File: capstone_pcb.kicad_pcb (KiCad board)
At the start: 4 copper layers, 60.2 x 43.6 mm, 44 parts, among them IC6 BSS138, Q1 BSS138, U2 BMI270, U3 NRF52840-QIAA-R, U4 MAX30102EFD+T, U5 AMS1117-1.8, U6 TPS61099DRV, X1 32MHz, X2 32.768kHz

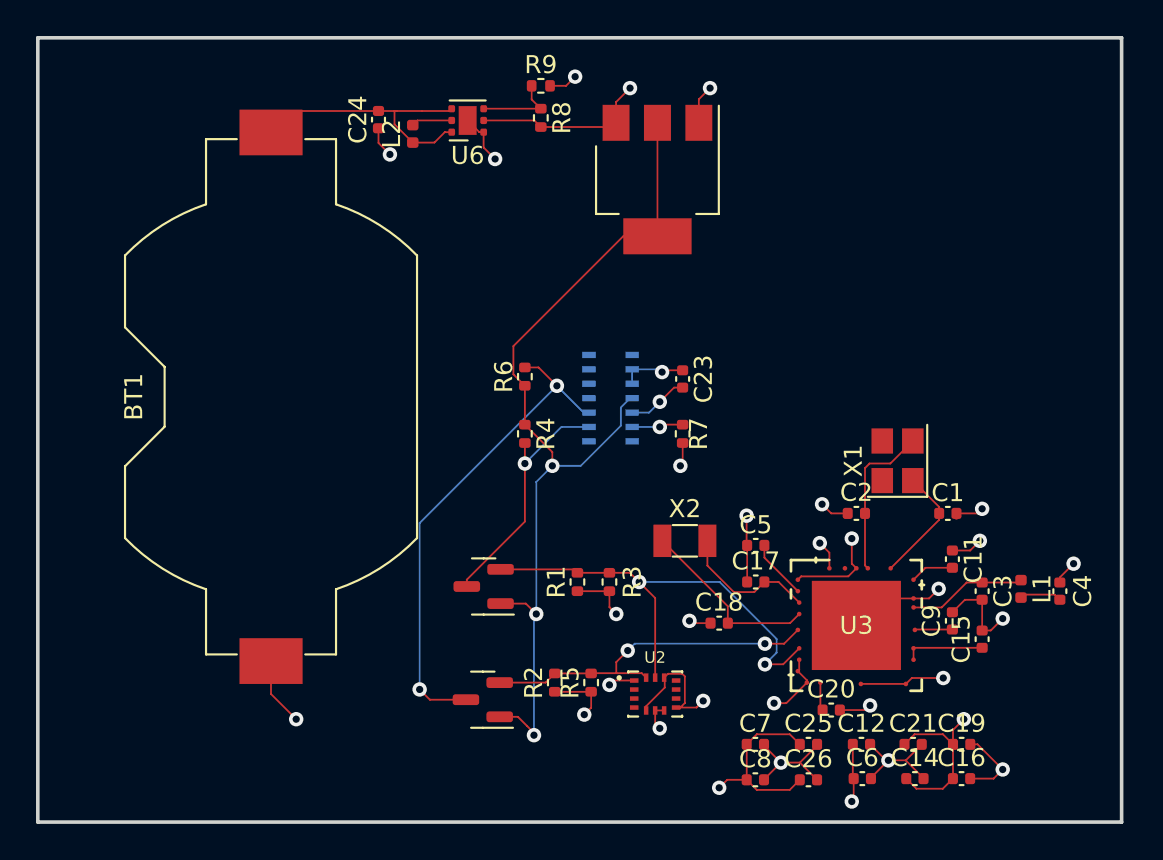
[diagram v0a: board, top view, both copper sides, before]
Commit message: exposed SWD pins and added LED for flashing status
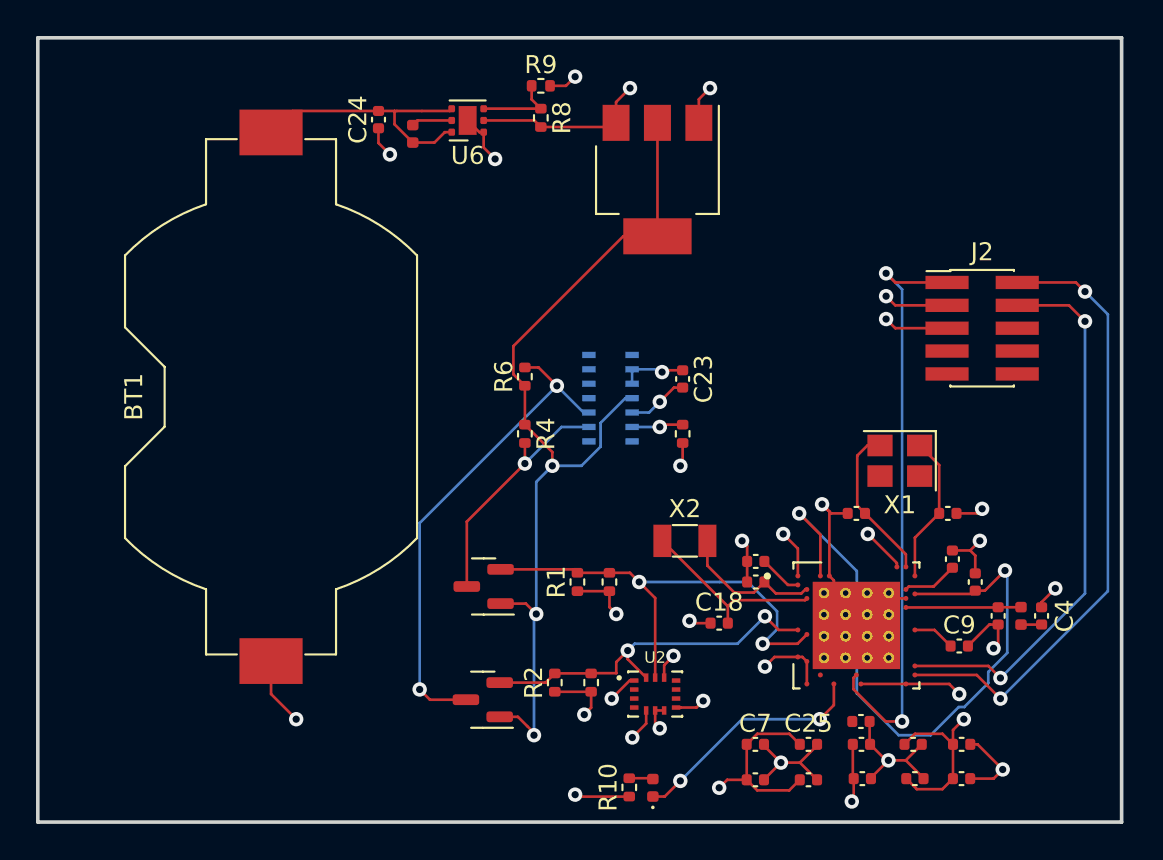
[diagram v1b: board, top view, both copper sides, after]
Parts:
- added D1: LED, LED_SMD:LED_0402_1005Metric, F.Cu at (114.6, 87.4)
- added J2: Conn_01x05_Pin, Connector_PinHeader_1.27mm:PinHeader_2x05_P1.27mm_Vertical_SMD, F.Cu at (132.8, 61.8)
- added R10: 0.4k, Resistor_SMD:R_0402_1005Metric, F.Cu at (113.2, 87.4)
- R3, R4, R5, R6, R7: value 10K -> 10k
- U3: footprint nrf:nrf52840_qiaa_r -> nrf:XCVR_NRF52840-QIAA-R-edited
- moved C15 3.20 mm to (132.5, 75.9)
- moved C20 1.77 mm to (126.1, 83.7)
- moved C4 1.71 mm to (136.1, 77.8)
- moved C3 1.64 mm to (133.7, 77.8)
- moved L1 1.50 mm to (135.0, 77.8)
- moved C9 1.45 mm to (131.6, 79.5), turned to 0 degrees
- moved C5 0.89 mm to (120.3, 74.8)
- moved X1 0.13 mm to (128.3, 69.2), turned to 180 degrees
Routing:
- net Net-(J2-Pin_2): track 0.00 -> 34.9 mm, vias 0 -> 2
- net Net-(J2-Pin_1): track 0.00 -> 33.2 mm, vias 0 -> 2
- net /DEC4 6: track 4.46 -> 37.0 mm, vias 0 -> 2
- net Net-(J2-Pin_4): track 0.00 -> 30.9 mm, vias 0 -> 2
- net Net-(D1-K): track 0.00 -> 13.3 mm, vias 0 -> 2
- net GND: track 61.4 -> 72.9 mm, vias 21 -> 19
- net +3V3: track 62.5 -> 68.0 mm, vias 11 -> 16
- net Net-(U3-XC1): track 6.59 -> 8.25 mm
- net Net-(U3-DECUSB): track 1.57 -> 0.00 mm
- net Net-(D1-A): track 0.00 -> 1.33 mm
- net /RF: track 2.28 -> 1.15 mm
- net Net-(U3-DEC1): track 3.31 -> 2.40 mm
- net /SDA: track 19.9 -> 20.7 mm
- net Net-(U3-DEC3): track 2.43 -> 3.08 mm

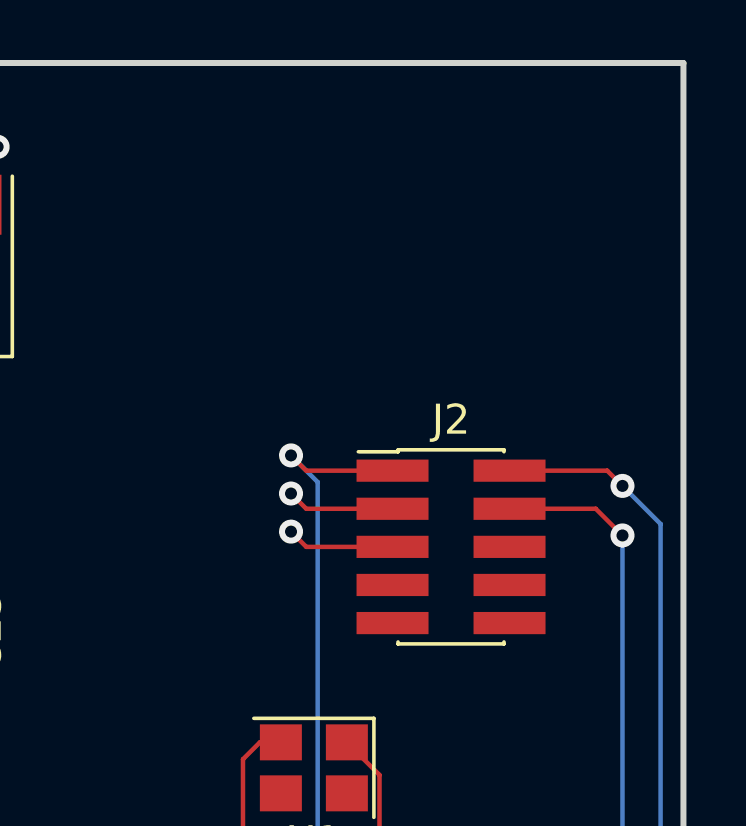
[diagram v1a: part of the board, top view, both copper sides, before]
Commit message: changed pin header
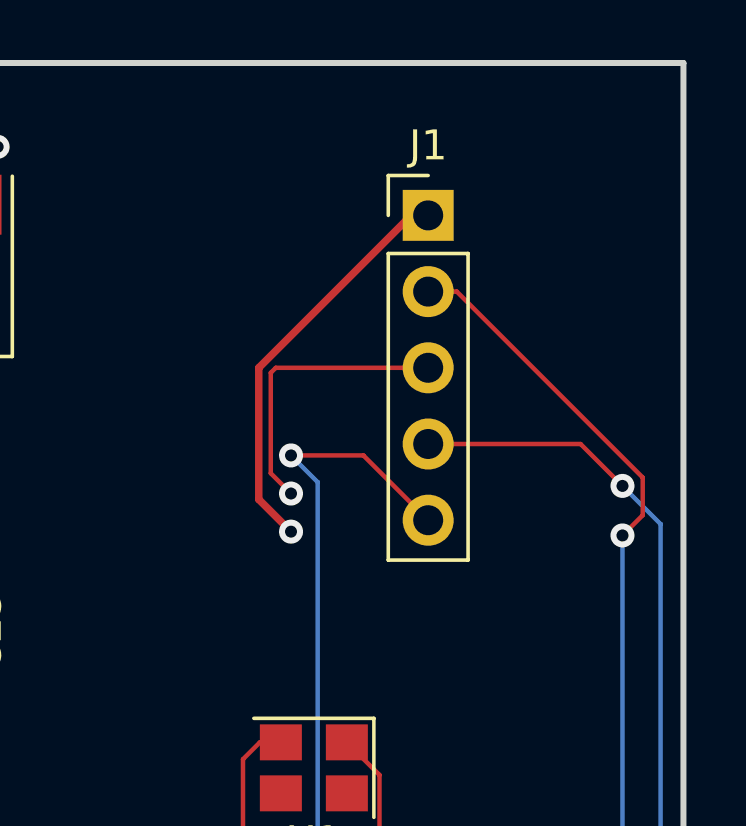
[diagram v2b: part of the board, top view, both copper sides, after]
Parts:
- removed J2: Conn_01x05_Pin, Connector_PinHeader_1.27mm:PinHeader_2x05_P1.27mm_Vertical_SMD
- added J1: Conn_01x05, Connector_PinHeader_2.54mm:PinHeader_1x05_P2.54mm_Vertical, F.Cu at (132.1, 50.8)
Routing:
- net +3V3: track 68.0 -> 78.0 mm
- net Net-(J1-Pin_2): track 30.9 -> 38.7 mm
- net GND: track 72.9 -> 79.0 mm
- net Net-(J1-Pin_4): track 34.9 -> 38.0 mm
- net Net-(J1-Pin_5): track 33.2 -> 35.2 mm

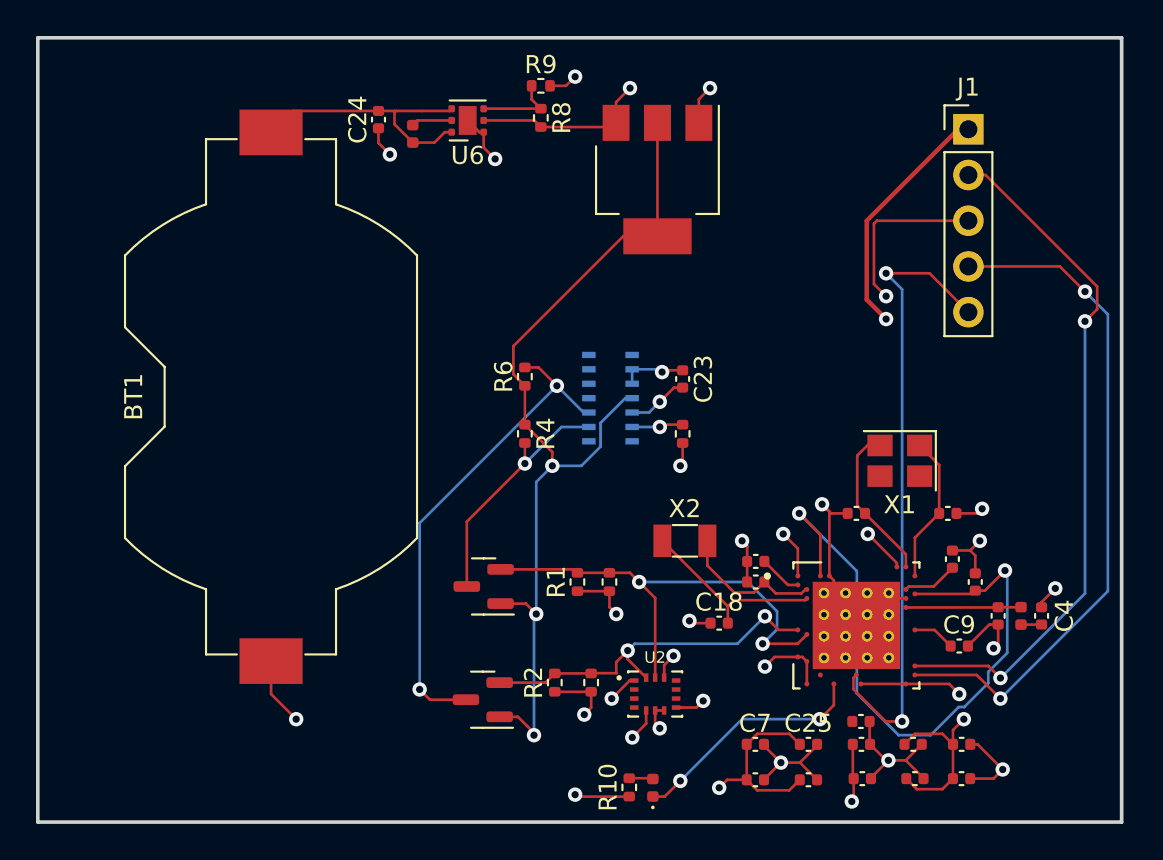
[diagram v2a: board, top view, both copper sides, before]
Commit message: add silkscreen labels to pin header
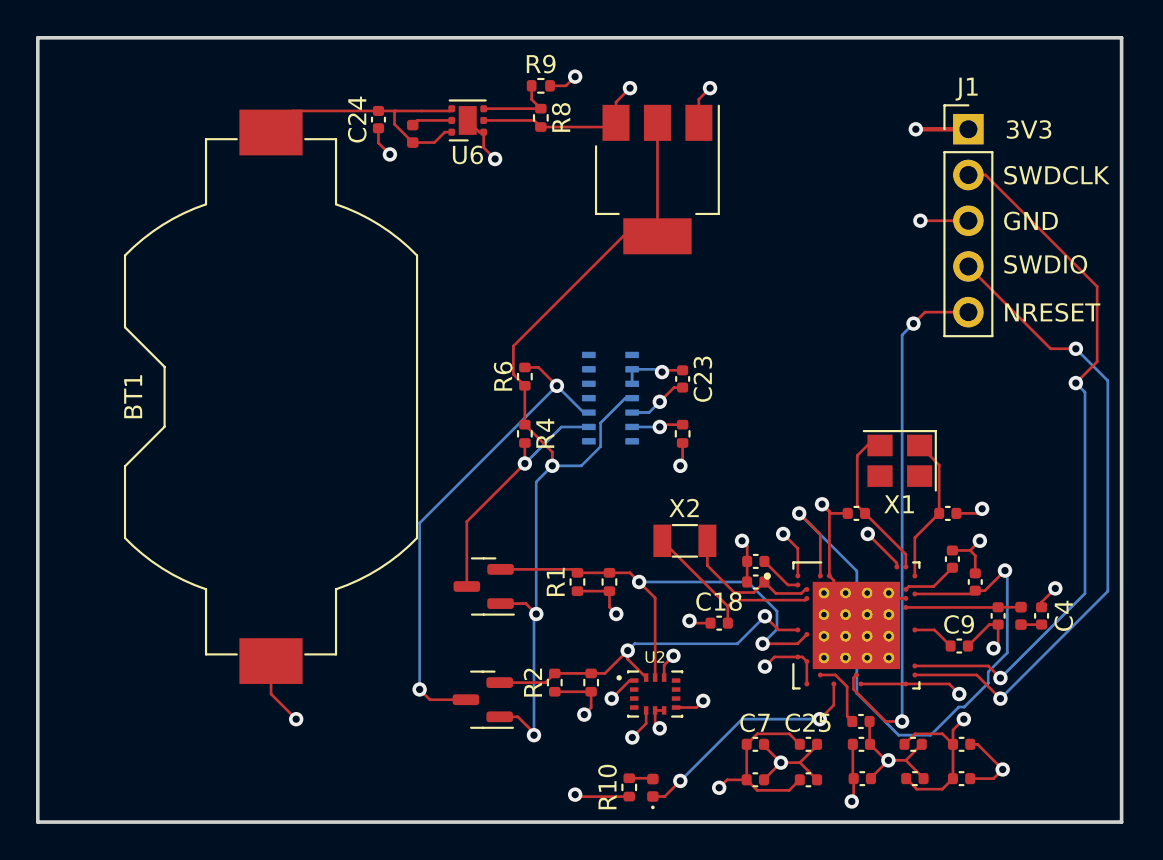
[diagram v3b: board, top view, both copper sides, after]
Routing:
- net +3V3: track 78.0 -> 67.3 mm
- net GND: track 79.0 -> 72.0 mm
- net Net-(J1-Pin_5): track 35.2 -> 30.0 mm
- net Net-(U3-DECUSB): track 0.00 -> 3.81 mm
- net Net-(J1-Pin_4): track 38.0 -> 35.8 mm
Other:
- board text added: "3V3"
- board text added: "GND"
- board text added: "NRESET"
- board text added: "SWDCLK"
- board text added: "SWDIO"

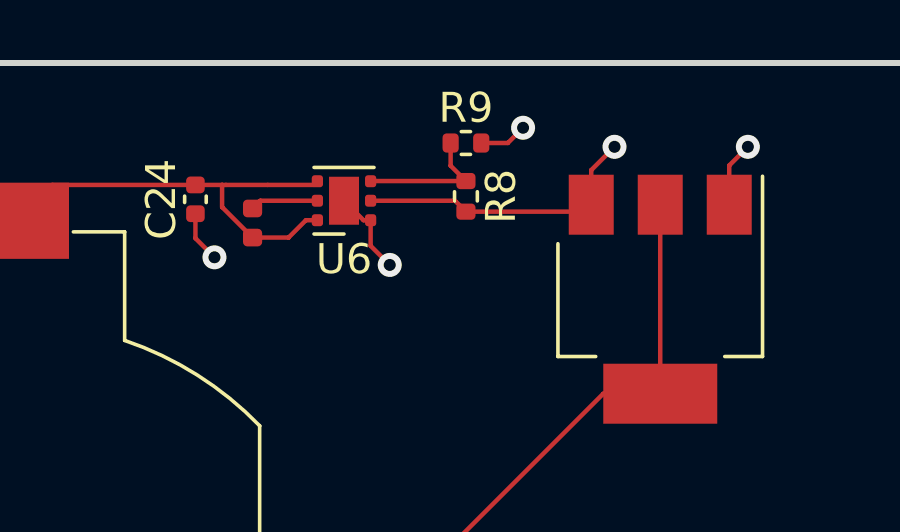
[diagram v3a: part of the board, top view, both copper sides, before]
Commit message: added 100k and 130k resistors in series
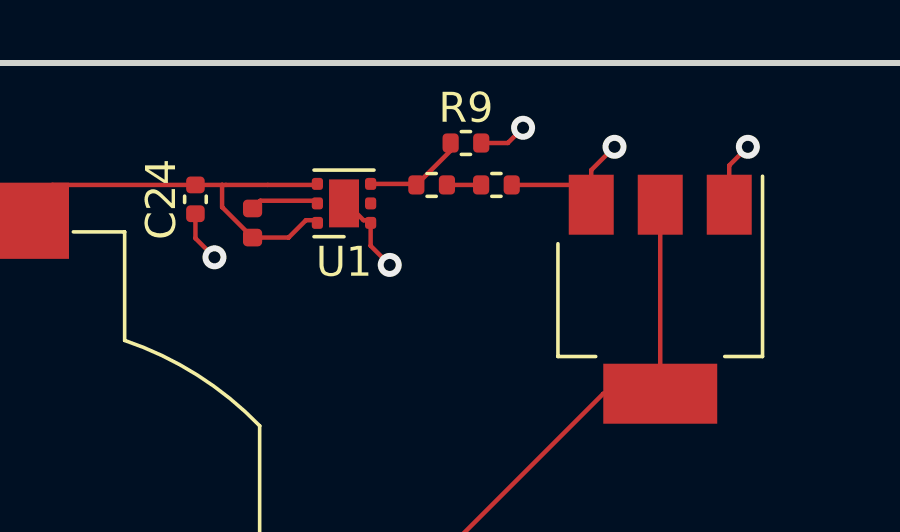
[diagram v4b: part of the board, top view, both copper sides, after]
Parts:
- removed U6: TPS61099DRV, Package_SON:WSON-6-1EP_2x2mm_P0.65mm_EP1x1.6mm
- added R11: 130k, Resistor_SMD:R_0402_1005Metric, F.Cu at (109.3, 49.8)
- added U1: TPS610994DRV, Package_SON:WSON-6-1EP_2x2mm_P0.65mm_EP1x1.6mm, F.Cu at (104.3, 50.4)
- R8: value 453k -> 100k
- moved R8 1.20 mm to (107.2, 49.8), turned to 180 degrees
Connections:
- R8 pad 1: Net-(U6-FB) -> Net-(R11-Pad2)
- R8 pad 2: +3V3 -> Net-(U1-FB)
- R9 pad 1: Net-(U6-FB) -> Net-(U1-FB)
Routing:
- net Net-(U6-FB): track 4.66 -> 0.00 mm
- net +3V3: track 67.3 -> 62.9 mm
- net Net-(U1-FB): track 0.00 -> 3.42 mm
- net Net-(R11-Pad2): track 0.00 -> 1.14 mm

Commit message: add 3.3v wire
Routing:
- net +3V3: track 62.9 -> 64.5 mm, vias 16 -> 17
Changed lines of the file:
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@@
   (segment (start 112.141 76.456) (end 110.363 76.456) (width 0.15) (layer "F.Cu") (net 8))
   (segment (start 116.081 82.919) (end 115.8435 82.919) (width 0.15) (layer "F.Cu") (net 8))
+  (segment (start 105.1545 50.4) (end 105.645 50.4) (width 0.15) (layer "F.Cu") (net 8))
   (segment (start 112.277 50.675) (end 112.508 50.444) (width 0.15) (layer "F.Cu") (net 8))
   (segment (start 125.707 88.034) (end 125.603 88.138) (width 0.15) (layer "F.Cu") (net 8))
@@
   (segment (start 119.766 84.963) (end 119.766 86.933) (width 0.15) (layer "F.Cu") (net 8))
   (segment (start 125.707 86.868) (end 125.707 88.034) (width 0.15) (layer "F.Cu") (net 8))
+  (segment (start 105.645 50.4) (end 106.426 51.181) (width 0.15) (layer "F.Cu") (net 8))
   (segment (start 123.107 81.609) (end 123.107 80.359) (width 0.15) (layer "F.Cu") (net 8))
   (segment (start 122.13 87.518) (end 122.715 86.933) (width 0.15) (layer "F.Cu") (net 8))
@@
   (via (at 118.237 87.376) (size 0.8) (drill 0.4) (layers "F.Cu" "B.Cu") (net 8))
   (via (at 113.284 48.514) (size 0.8) (drill 0.4) (layers "F.Cu" "B.Cu") (net 8))
+  (via (at 106.426 51.181) (size 0.8) (drill 0.4) (layers "F.Cu" "B.Cu") (net 8))
   (via (at 116.081 69.494) (size 0.8) (drill 0.4) (layers "F.Cu" "B.Cu") (net 8))
   (via (at 115.697 80.0495) (size 0.8) (drill 0.4) (layers "F.Cu" "B.Cu") (net 8))

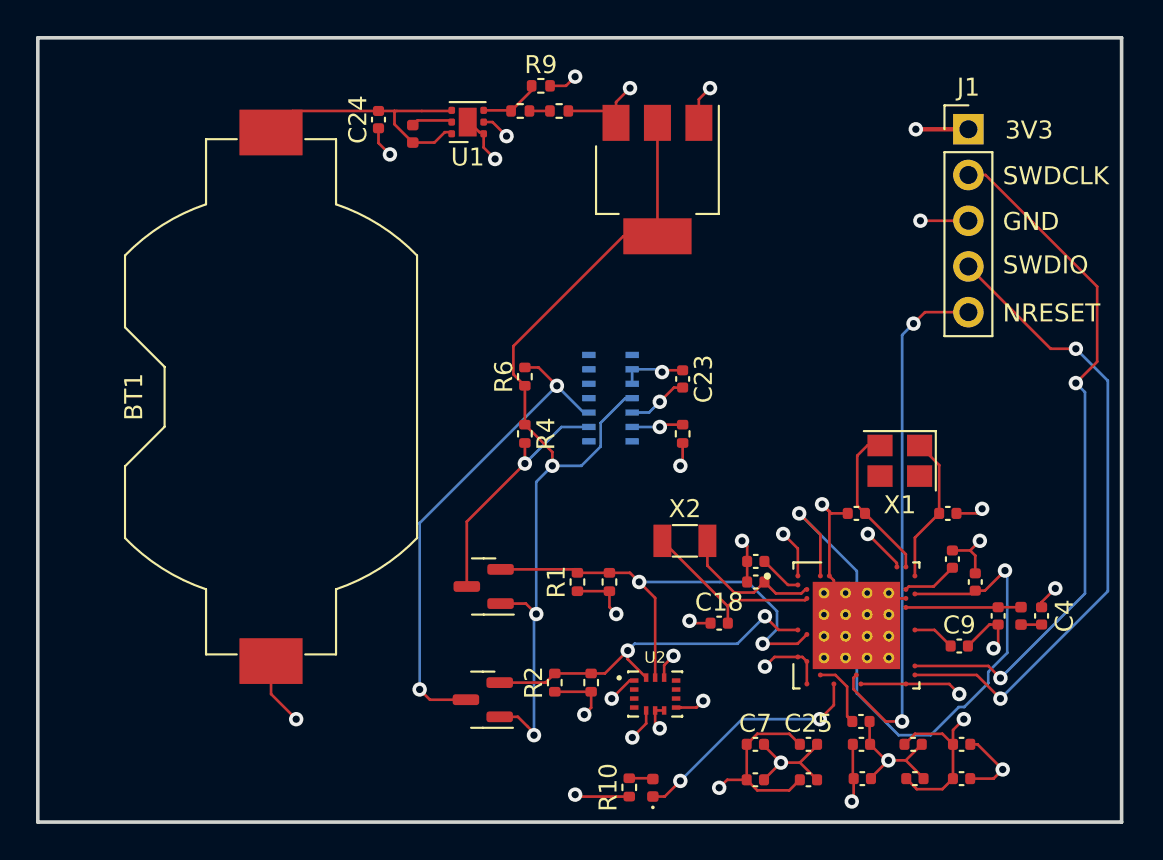
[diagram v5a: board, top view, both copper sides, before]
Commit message: rearrange cap. and resist. to correct locations
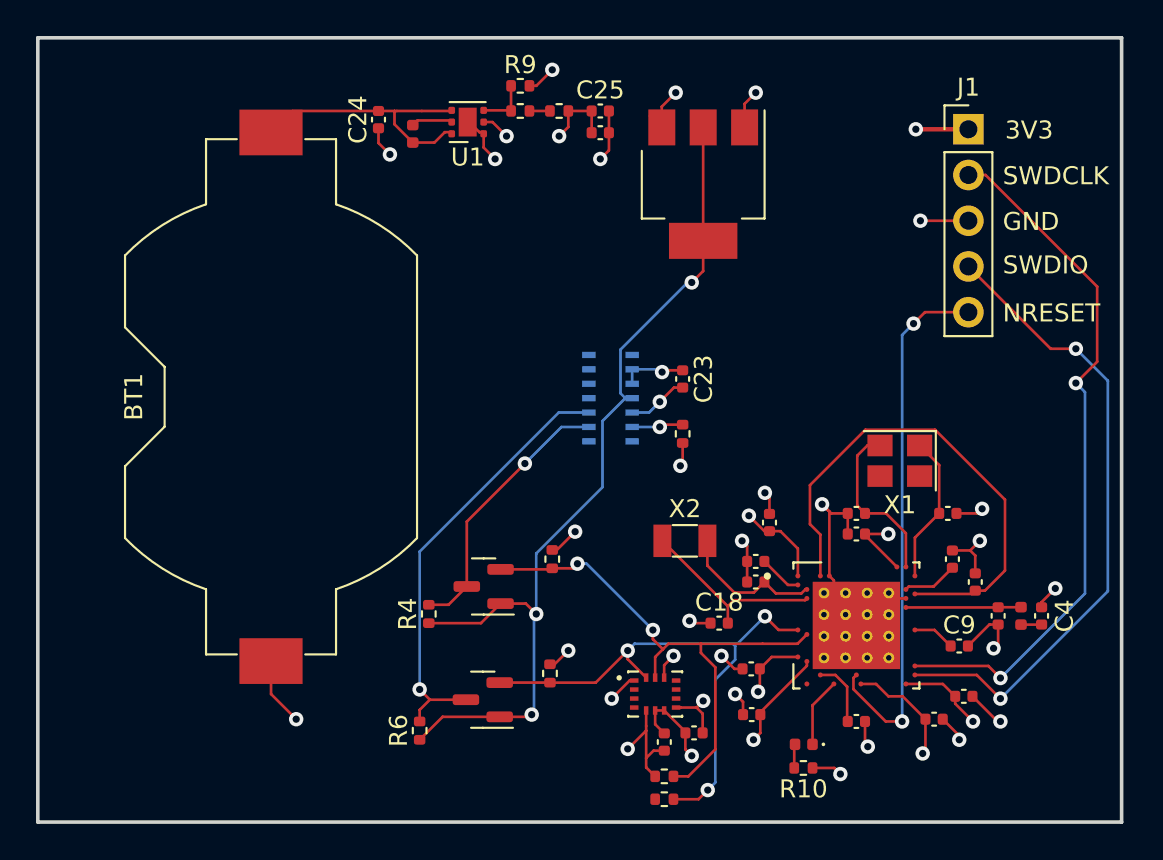
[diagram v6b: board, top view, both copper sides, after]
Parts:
- moved C26 37.8 mm to (111.6, 51.0)
- moved C25 37.0 mm to (111.6, 49.8)
- moved R6 20.5 mm to (101.6, 84.2)
- moved C14 16.4 mm to (121.0, 72.6), turned to 90 degrees
- moved C16 15.1 mm to (116.8, 84.3), turned to 180 degrees
- moved C21 13.8 mm to (115.2, 84.8), turned to 90 degrees
- moved C8 12.5 mm to (131.8, 82.3)
- moved R1 11.8 mm to (115.2, 86.7), turned to 0 degrees
- moved C19 11.8 mm to (120.0, 83.3), turned to 180 degrees
- moved C12 11.7 mm to (125.9, 73.3), turned to 180 degrees
- moved R4 11.3 mm to (102.1, 77.7), turned to 90 degrees
- moved C7 10.0 mm to (130.2, 83.6)
- moved R10 9.73 mm to (122.9, 86.3), turned to 180 degrees
- moved R2 8.89 mm to (115.2, 88.0), turned to 0 degrees
- moved D1 8.72 mm to (122.9, 85.0), turned to 180 degrees
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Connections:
- U3 pad AD2: +3V3 -> /AD2
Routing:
- net /SDA: track 20.3 -> 31.5 mm, vias 2 -> 3
- net Net-(D1-K): track 13.3 -> 3.85 mm, vias 2 -> 0
- net /DEC4 6: track 37.0 -> 28.5 mm, vias 2 -> 0
- net +3V3: track 64.5 -> 58.8 mm
- net /SCL: track 26.8 -> 30.6 mm
- net /BSDA: track 27.4 -> 24.5 mm, vias 2 -> 1
- net GND: track 72.0 -> 70.1 mm, vias 19 -> 23
- net /BSCL: track 13.9 -> 15.3 mm
- net Net-(U3-XC2): track 8.80 -> 9.48 mm
